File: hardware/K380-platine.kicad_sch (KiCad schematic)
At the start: 39 parts, among them J1 JST-PH 2, J2 Conn_01x23, J3 MicroMod-M.2E, J4 USB_C_Receptacle_USB2.0, J5 Conn_ARM_JTAG_SWD_10, Q1 PMost Enc FET -20V, Q2 Q_NMOS_DGS, SW1 EG1215AA, SW2 SW_Push, SW3 SW_Push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

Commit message: hardware: update WS2812B 2020 symbol [unrooted]
Previously the footprint and symbol pinout didn't match the WS2812B 2020
datasheet. I previously thought that I could get away with just using
the WS2812B symbol, but in my blissful ignorance I didn't notice that
the WS2812B symbol has a different ordering of the number pins.

This patch introduces a new WS2812B_2020 symbol in LibraryLoader, which
is a copy of the WS2812B symbol, but with the pinout from the datasheet.

Signed-off-by: Sophie Friedrich <dev@flowerpot.me>
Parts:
- D3, D4, D5, D6: symbol LED:WS2812B -> LibraryLoader:WS2812B_2020
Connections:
- net +3V3: now also D3.4 (VDD), D4.4 (VDD), D5.4 (VDD), D6.4 (VDD); no longer D3.1 (VDD), D4.1 (VDD), D5.1 (VDD), D6.1 (VDD)
- net DLED: now also D3.3 (DIN); no longer D3.4 (DIN)
- net GND: now also D3.2 (VSS), D4.2 (VSS), D5.2 (VSS), D6.2 (VSS); no longer D3.3 (VSS), D4.3 (VSS), D5.3 (VSS), D6.3 (VSS)
- new net: D5.1 (DOUT), D6.3 (DIN)
- new net: D4.1 (DOUT), D5.3 (DIN)
- new net: D3.1 (DOUT), D4.3 (DIN)
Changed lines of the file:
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@@
     )
   )
-  (symbol (lib_id "LED:WS2812B") (at 374.65 182.88 180) (unit 1)
+  (symbol (lib_id "LibraryLoader:WS2812B_2020") (at 374.65 182.88 180) (unit 1)
     (in_bom yes) (on_board yes) (dnp no)
     (property "Reference" "D6" (at 383.3876 181.7116 0)
@@
       (effects (font (size 1.27 1.27)) (justify left top) hide)
     )
-    (property "Datasheet" "https://cdn-shop.adafruit.com/datasheets/WS2812B.pdf" (at 372.11 173.355 0)
+    (property "Datasheet" "https://cdn-shop.adafruit.com/product-files/4684/4684_WS2812B-2020_V1.3_EN.pdf" (at 372.11 173.355 0)
       (effects (font (size 1.27 1.27)) (justify left top) hide)
     )
@@
     )
   )
-  (symbol (lib_id "LED:WS2812B") (at 374.65 158.75 0) (unit 1)
+  (symbol (lib_id "LibraryLoader:WS2812B_2020") (at 374.65 158.75 0) (unit 1)
     (in_bom yes) (on_board yes) (dnp no)
     (property "Reference" "D5" (at 383.3876 157.5816 0)
@@
       (effects (font (size 1.27 1.27)) (justify left top) hide)
     )
-    (property "Datasheet" "https://cdn-shop.adafruit.com/datasheets/WS2812B.pdf" (at 377.19 168.275 0)
+    (property "Datasheet" "https://cdn-shop.adafruit.com/product-files/4684/4684_WS2812B-2020_V1.3_EN.pdf" (at 377.19 168.275 0)
       (effects (font (size 1.27 1.27)) (justify left top) hide)
     )
@@
     )
   )
-  (symbol (lib_id "LED:WS2812B") (at 353.06 158.75 0) (unit 1)
+  (symbol (lib_id "LibraryLoader:WS2812B_2020") (at 353.06 158.75 0) (unit 1)
     (in_bom yes) (on_board yes) (dnp no)
     (property "Reference" "D4" (at 361.7976 157.5816 0)
@@
       (effects (font (size 1.27 1.27)) (justify left top) hide)
     )
-    (property "Datasheet" "https://cdn-shop.adafruit.com/datasheets/WS2812B.pdf" (at 355.6 168.275 0)
+    (property "Datasheet" "https://cdn-shop.adafruit.com/product-files/4684/4684_WS2812B-2020_V1.3_EN.pdf" (at 355.6 168.275 0)
       (effects (font (size 1.27 1.27)) (justify left top) hide)
     )
@@
     )
   )
-  (symbol (lib_id "LED:WS2812B") (at 330.2 158.75 0) (unit 1)
+  (symbol (lib_id "LibraryLoader:WS2812B_2020") (at 330.2 158.75 0) (unit 1)
     (in_bom yes) (on_board yes) (dnp no)
     (property "Reference" "D3" (at 338.9376 157.5816 0)
@@
       (effects (font (size 1.27 1.27)) (justify left top) hide)
     )
-    (property "Datasheet" "https://cdn-shop.adafruit.com/datasheets/WS2812B.pdf" (at 332.74 168.275 0)
+    (property "Datasheet" "https://cdn-shop.adafruit.com/product-files/4684/4684_WS2812B-2020_V1.3_EN.pdf" (at 332.74 168.275 0)
       (effects (font (size 1.27 1.27)) (justify left top) hide)
     )

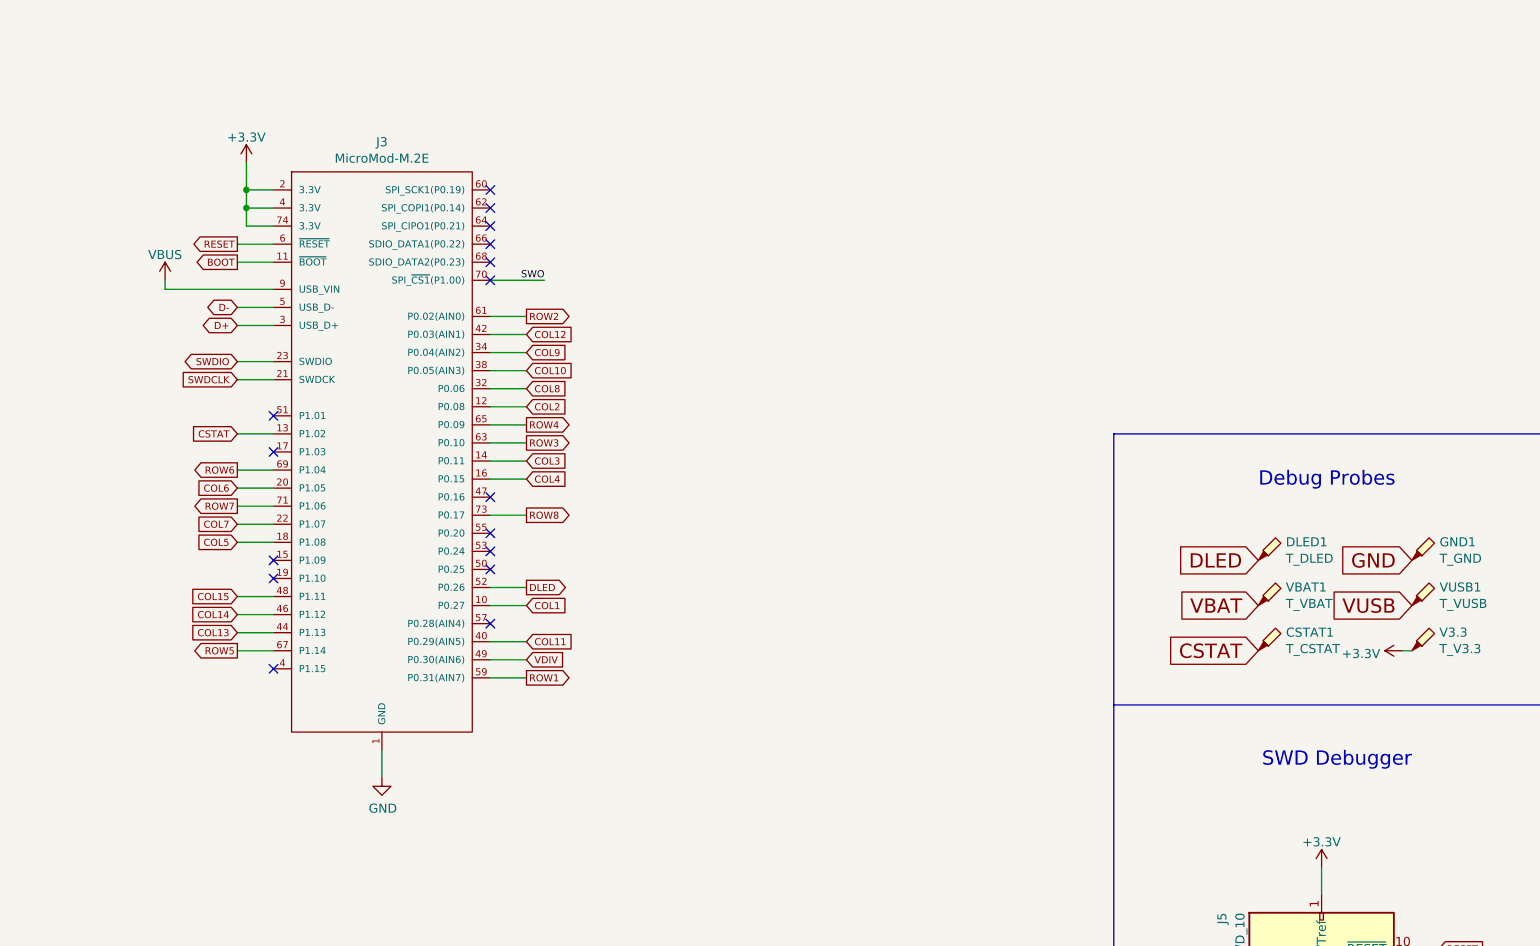
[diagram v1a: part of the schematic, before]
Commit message: hardware: schematic: Moved MCU to separate page
With this separation of content, it will make the future change of
directly placing the nRF52840 module onto the board much easier, as all
parts that replace the micromod module will be part of this new sheet.

Signed-off-by: Sophie Friedrich <dev@flowerpot.me>
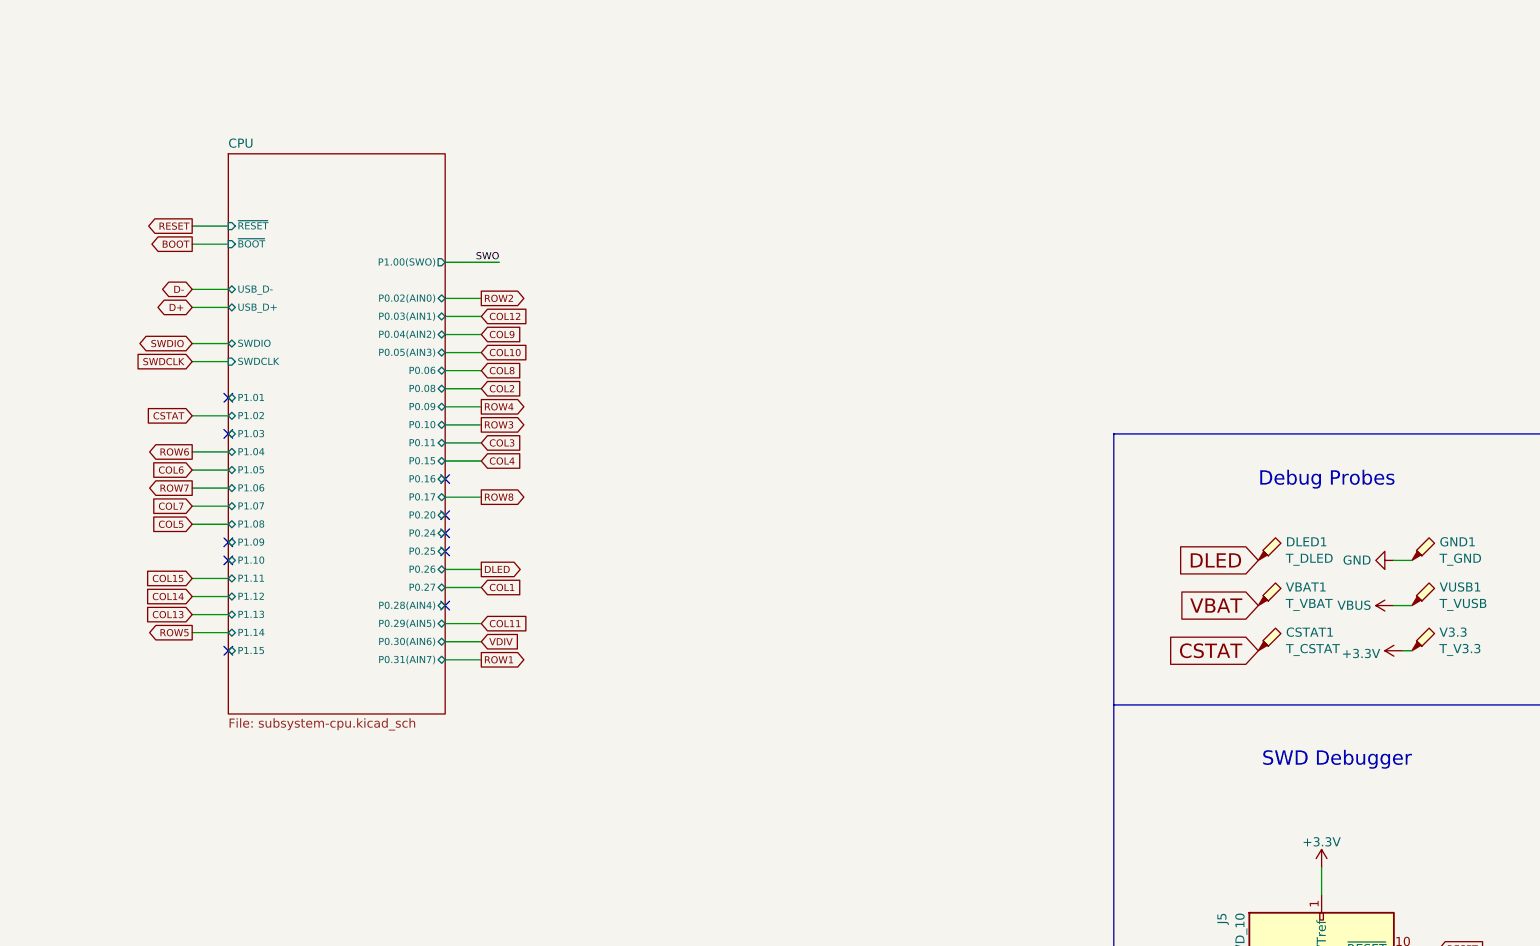
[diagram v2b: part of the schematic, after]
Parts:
- removed J3: MicroMod-M.2E, SparkFun MicroMod:M.2-CONNECTOR-E, symbol custom_footprints:MicroMod-M.2E
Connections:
- net VUSB is gone; now on net VBUS: VUSB1.1
- no-connect marks 23 -> 17
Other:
- added sheet CPU (subsystem-cpu.kicad_sch)

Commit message: hardware: first nRF52840 raw tries
The current schematic should (in theory) be a complete setup for the
nRF52840 chip with power and everything.

In the footprint first routing attempts have been made, but this has
been without real success for now, especially as the nRF52840 is a hell
of a chip to implement. Ignoring the whole "need to do own RF" here,
it's almost impossible to get the inner pins out from under the chip
without paying extra for either via-in-pads or precision milling.

I'll leave this commit here for an exemplary routing of (some) inner
GPIO pins off the nRF52840 while presumably being in spec of JLCPCBs
capabilities. I want this project to come to an end, so I'll step away
from implementing my own nRF52840, and buy a carrier module with it
instead.

And yeah - RF stuff is magic and mostly consists of dark incantations.
The major advantage of buying a carrier board that already does the RF
for me, is that I have fewer requirements on the PCB manufacturer and
people can just manufacture it with their favorite producer.

Signed-off-by: Sophie Friedrich <dev@flowerpot.me>
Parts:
- removed J5: Conn_ARM_JTAG_SWD_10, Connector_PinHeader_1.27mm:PinHeader_2x05_P1.27mm_Vertical_SMD, symbol Connector:Conn_ARM_JTAG_SWD_10
- U2: footprint Package_TO_SOT_SMD:SOT-23-5_HandSoldering -> Package_TO_SOT_SMD:SOT-23-5
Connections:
- net VBAT is gone; now on net +BATT: VBAT1.1
- net +3V3 renamed +3.3V
- no-connect marks 17 -> 15
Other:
- sheet CPU ports: added none; removed P1.00(SWO), SWDCLK, SWDIO
- note removed: "SWD Debugger"

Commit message: Revert "hardware: first nRF52840 raw tries"
Wanna start from a clean slate. See referenced commit on why I'm doing
this.

This reverts commit 5420c1d1e1bdfd9146d776c48bdd16e2d166426d.
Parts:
- added J5: Conn_ARM_JTAG_SWD_10, Connector_PinHeader_1.27mm:PinHeader_2x05_P1.27mm_Vertical_SMD, symbol Connector:Conn_ARM_JTAG_SWD_10
- U2: footprint Package_TO_SOT_SMD:SOT-23-5 -> Package_TO_SOT_SMD:SOT-23-5_HandSoldering
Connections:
- net +BATT: no longer VBAT1.1
- net GND: now also J5.3 (GND), J5.5 (GND), J5.9 (GNDDetect)
- net RESET: now also J5.10 (~{RESET})
- net +3.3V renamed +3V3
- net +3V3: now also J5.1 (VTref)
- new net SWDCLK: J5.4 (SWDCLK/TCK)
- new net SWDIO: J5.2 (SWDIO/TMS)
- new net SWO: J5.6 (SWO/TDO)
- new net VBAT: VBAT1.1
- no-connect marks 15 -> 17
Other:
- sheet CPU ports: added P1.00(SWO), SWDCLK, SWDIO; removed none
- note added: "SWD Debugger"

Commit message: hardware: completed rev 0.2α (pre-verify)
This is a bigger change from the iteration. The MicroMod has been
replaced with an HolyIoT nRF52840, which can be directly soldered onto
the board. This guarantees minimal space usage, while reducing the
complexity to implement an MCU on our own.

Additionally this iteration moves away from reserving a gpio port per
keyboard matrix trace, and instead makes use of an GPIO shift register
(74AHC595A). They are quite popular and also have support in ZMK since a
few weeks ago.

This commit adheres to the design rules for a 2 layer PCB and passes all
DRC checks.

Signed-off-by: Sophie Friedrich <dev@flowerpot.me>
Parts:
- removed SW3: SW_Push, LibraryLoader:MJTP1140AAUTR - Fixed, symbol Switch:SW_Push
- added C7: 100uF, Capacitor_SMD:C_0603_1608Metric_Pad1.08x0.95mm_HandSolder, symbol Device:C
- added H1, H2: MountingHole, MountingHole:MountingHole_3.2mm_M3_DIN965_Pad, symbol Mechanical:MountingHole
- added R10: 10k, Capacitor_SMD:C_0603_1608Metric_Pad1.08x0.95mm_HandSolder, symbol Device:R_Small
- added U3: nRF52840_holyiot_18010, PCM_marbastlib-various:nRF52840_holyiot_18010_HS_simple, symbol PCM_marbastlib-various:nRF52840_holyiot_18010
- added U4, U5: 74AHC595, Package_SO:TSSOP-16_4.4x5mm_P0.65mm, symbol 74xx:74AHC595
- U2: footprint Package_TO_SOT_SMD:SOT-23-5_HandSoldering -> Package_TO_SOT_SMD:SOT-23-5
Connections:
- net VBAT is gone; now on net +BATT: VBAT1.1
- net COL1: now also U5.15 (QA)
- net COL10: now also U4.1 (QB)
- net COL11: now also U4.2 (QC)
- net COL12: now also U4.3 (QD)
- net COL13: now also U4.4 (QE)
- net COL14: now also U4.5 (QF)
- net COL15: now also U4.6 (QG)
- net COL2: now also U5.1 (QB)
- net COL3: now also U5.2 (QC)
- net COL4: now also U5.3 (QD)
- net COL5: now also U5.4 (QE)
- net COL6: now also U5.5 (QF)
- net COL7: now also U5.6 (QG)
- net COL8: now also U5.7 (QH)
- net COL9: now also U4.15 (QA)
- net CSTAT: now also U3.12 (P0.04-A)
- net D+: now also U3.24 (D+)
- net D-: now also U3.23 (D-)
- net DLED: now also U3.20 (P0.19)
- net GND: now also C7.2, U3.1 (GND), U3.25 (GND), U3.37 (GND), U4.13 (~{OE}), U4.8 (GND), U5.13 (~{OE}), U5.8 (GND)
- net RESET: now also R10.2, U3.21 (P0.18-RESET)
- net ROW1: now also U3.26 (P0.22)
- net ROW2: now also U3.28 (P1.03-LF)
- net ROW3: now also U3.29 (P1.01-LF)
- net ROW4: now also U3.30 (P1.02-LF)
- net ROW5: now also U3.33 (P1.04-LF)
- net ROW6: now also U3.34 (P1.06-LF)
- net ROW7: now also U3.35 (P0.09-LF-NFC)
- net ROW8: now also U3.36 (P0.10-LF-NFC)
- net SWDCLK: now also U3.31 (SWDCLK)
- net SWDIO: now also U3.32 (SWDIO)
- net SWO: now also U3.27 (P1.00)
- net VBUS: now also U3.22 (VBUS)
- net VDIV: now also U3.13 (P0.05-A)
- net +3V3 renamed +3.3V
- net +3.3V: now also C7.1, R10.1, U3.14 (VDD_nRF), U4.10 (~{SRCLR}), U4.16 (VCC), U5.10 (~{SRCLR}), U5.16 (VCC)
- new net: U4.14 (SER), U5.9 (QH')
- new net LS_EN: U3.16 (P1.09), U4.12 (RCLK), U5.12 (RCLK)
- new net LS_MOSI: U3.17 (P0.12), U5.14 (SER)
- new net LS_SCK: U3.15 (P0.07), U4.11 (SRCLK), U5.11 (SRCLK)
- no-connect marks 17 -> 38
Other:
- removed sheet CPU
- note added: "Brain"
- note added: "GPIO shift register for keyboard matrix"
- moved on the sheet: C6, CSTAT1, DLED1, GND1, SW2, V3.3, VBAT1, VUSB1
